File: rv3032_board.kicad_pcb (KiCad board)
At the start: 2 copper layers, 13.8 x 14.5 mm, 7 parts, among them J1 Conn_01x05_Pin, U1 RV-3032

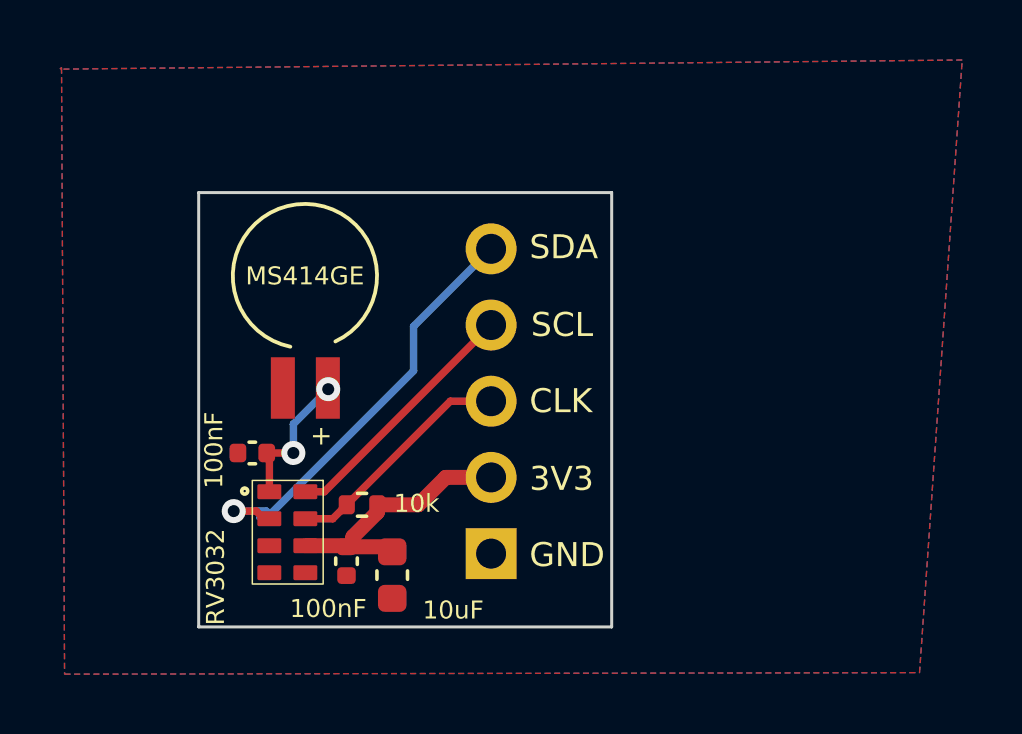
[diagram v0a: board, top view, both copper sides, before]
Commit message: v2: replacement DS3231
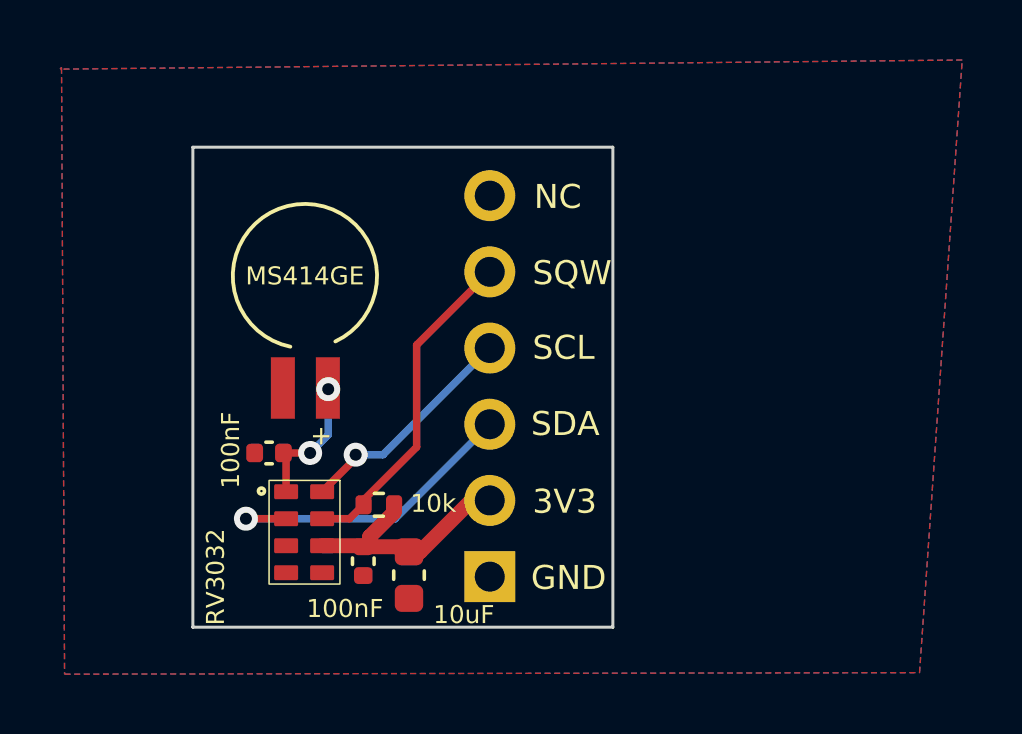
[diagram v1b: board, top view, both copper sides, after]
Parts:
- J1: value Conn_01x05_Pin -> Conn_01x06_Pin; footprint Connector_PinHeader_2.54mm:PinHeader_1x05_P2.54mm_Horizontal -> Connector_PinHeader_2.54mm:PinHeader_1x06_P2.54mm_Horizontal
- moved J1 0.77 mm to (164.9, 80.3)
- moved C3 0.56 mm to (157.5, 76.2)
- moved R1 0.56 mm to (161.2, 77.9)
- moved C1 0.56 mm to (162.2, 80.3)
- moved C2 0.56 mm to (160.7, 79.8)
- moved U1 0.56 mm to (158.7, 78.8)
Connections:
- J1 pad 3: RTC_SQW -> I2C_SDA_OTHER
- J1 pad 5: I2C_SDA_OTHER -> RTC_SQW
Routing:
- net I2C_SDA_OTHER: track 15.0 -> 10.8 mm
- net RTC_SQW: track 7.81 -> 11.1 mm
- net +3V3: track 8.92 -> 8.15 mm
- net I2C_SCL_OTHER: track 8.49 -> 7.75 mm, vias 0 -> 1
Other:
- board size 13.8 x 14.5 mm -> 14 x 16 mm
- board text added: "NC"
- board text added: "SQW"
- board text removed: "CLK"

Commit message: v1 ordered
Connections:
- J1 pad 6: unconnected-(J1-Pin_6-Pad6) -> RTC_INT
- U1 pad 3: unconnected-(U1-~{INT}-Pad3) -> RTC_INT
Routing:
- net RTC_INT: track 0.00 -> 20.4 mm, vias 0 -> 1
- net Net-(BT1-+): track 4.59 -> 4.63 mm, vias 2 -> 0
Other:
- board text added: "INT"
- board text added: "V1"
- board text removed: "NC"
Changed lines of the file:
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@@
   (net 4 "RTC_SQW")
   (net 5 "I2C_SDA_OTHER")
-  (net 6 "unconnected-(U1-~{INT}-Pad3)")
+  (net 6 "RTC_INT")
   (net 7 "unconnected-(U1-EVI-Pad4)")
   (net 8 "I2C_SCL_OTHER")
-  (net 9 "unconnected-(J1-Pin_6-Pad6)")
   (footprint "MyFootprints:BAT_MS414GE-FL26E" (layer "F.Cu")
     (at 158.75 70.3006 -90)
@@
         (effects (font (size 0.6 0.6) (thickness 0.15)))
     )
-    (fp_text user "+" (at 5.334 -0.508 90) (layer "F.SilkS")
+    (fp_text user "+" (at 3.7404 -1.7526 90) (layer "F.SilkS")
         (effects (font (size 0.64 0.64) (thickness 0.15)))
     )
@@
       (net 5 "I2C_SDA_OTHER") (pinfunction "SDA") (pintype "bidirectional") (thermal_bridge_angle 45))
     (pad "3" smd roundrect (at 0.45 0.6 90) (size 0.5 0.8) (layers "F.Cu" "F.Paste" "F.Mask") (roundrect_rratio 0.1)
-      (net 6 "unconnected-(U1-~{INT}-Pad3)") (pinfunction "~{INT}") (pintype "open_collector+no_connect") (thermal_bridge_angle 45))
+      (net 6 "RTC_INT") (pinfunction "~{INT}") (pintype "open_collector") (thermal_bridge_angle 45))
     (pad "4" smd roundrect (at 1.35 0.6 90) (size 0.5 0.8) (layers "F.Cu" "F.Paste" "F.Mask") (roundrect_rratio 0.1)
       (net 7 "unconnected-(U1-EVI-Pad4)") (pinfunction "EVI") (pintype "input+no_connect") (thermal_bridge_angle 45))
@@
         (effects (font (size 1 1) (thickness 0.15)))
     )
-    (fp_text value "10k" (at 1.8192 -0.0436) (layer "F.SilkS")
+    (fp_text value "10k" (at 1.7684 -0.5516) (layer "F.SilkS")
         (effects (font (size 0.6 0.6) (thickness 0.15)))
     )
@@
       (net 4 "RTC_SQW") (pinfunction "Pin_5") (pintype "passive"))
     (pad "6" thru_hole oval (at 0 -12.7) (size 1.7 1.7) (drill 1) (layers "*.Cu" "*.Mask")
-      (net 9 "unconnected-(J1-Pin_6-Pad6)") (pinfunction "Pin_6") (pintype "passive+no_connect"))
+      (net 6 "RTC_INT") (pinfunction "Pin_6") (pintype "passive"))
     (model "${KICAD6_3DMODEL_DIR}/Connector_PinHeader_2.54mm.3dshapes/PinHeader_1x06_P2.54mm_Horizontal.wrl"
       (offset (xyz 0 0 0))
@@
   (gr_rect (start 155 66) (end 169 82)
     (stroke (width 0.1) (type default)) (fill none) (layer "Edge.Cuts"))
-  (gr_text "RV3032" (at 162.306 69.5452) (layer "B.SilkS")
+  (gr_text "RV3032" (at 162.814 72.3646) (layer "B.SilkS")
     (effects (font (size 1 1) (thickness 0.15)) (justify left bottom mirror))
   )
-  (gr_text "NC" (at 166.37 68.1228) (layer "F.SilkS")
+  (gr_text "V1" (at 162.6616 74.0156) (layer "B.SilkS")
+    (effects (font (size 0.7 0.7) (thickness 0.1)) (justify left bottom mirror))
+  )
+  (gr_text "INT" (at 166.37 68.1228) (layer "F.SilkS")
     (effects (font (size 0.8 0.8) (thickness 0.15)) (justify left bottom))
   )
@@
     (style (thickness 0.15) (arrow_length 1.27) (text_position_mode 0) (extension_height 0.58642) (extension_offset 0.5) keep_text_aligned)
   )
+  (segment (start 159.5 75.601897) (end 159.5 74.0256) (width 0.25) (layer "F.Cu") (net 1))
   (segment (start 158.1088 76.2812) (end 158.0204 76.1928) (width 0.25) (layer "F.Cu") (net 1))
   (segment (start 158.1088 77.4844) (end 158.1088 76.2812) (width 0.25) (layer "F.Cu") (net 1))
+  (segment (start 158.909097 76.1928) (end 159.5 75.601897) (width 0.25) (layer "F.Cu") (net 1))
   (segment (start 158.0204 76.1928) (end 158.909097 76.1928) (width 0.25) (layer "F.Cu") (net 1))
-  (via (at 159.512 74.0664) (size 0.8) (drill 0.4) (layers "F.Cu" "B.Cu") (net 1))
-  (via (at 158.909097 76.1928) (size 0.8) (drill 0.4) (layers "F.Cu" "B.Cu") (net 1))
-  (segment (start 159.512 75.589897) (end 158.909097 76.1928) (width 0.25) (layer "B.Cu") (net 1))
-  (segment (start 159.512 74.0664) (end 159.512 75.589897) (width 0.25) (layer "B.Cu") (net 1))
   (segment (start 160.8932 78.9868) (end 161.708 78.172) (width 0.5) (layer "F.Cu") (net 3))
   (segment (start 160.858 79.2844) (end 160.8932 79.3196) (width 0.5) (layer "F.Cu") (net 3))
@@
   (segment (start 159.3088 78.3844) (end 160.2236 78.3844) (width 0.25) (layer "F.Cu") (net 4))
   (segment (start 162.4584 72.5932) (end 164.8968 70.1548) (width 0.25) (layer "F.Cu") (net 4))
-  (segment (start 158.1088 78.3844) (end 156.7688 78.3844) (width 0.25) (layer "F.Cu") (net 5))
-  (via (at 156.7688 78.3844) (size 0.8) (drill 0.4) (layers "F.Cu" "B.Cu") (net 5))
-  (segment (start 156.7688 78.3844) (end 161.7472 78.3844) (width 0.25) (layer "B.Cu") (net 5))
+  (segment (start 156.7434 78.1304) (end 156.9974 78.3844) (width 0.25) (layer "F.Cu") (net 5))
+  (segment (start 156.9974 78.3844) (end 158.1088 78.3844) (width 0.25) (layer "F.Cu") (net 5))
+  (via (at 156.7434 78.1304) (size 0.8) (drill 0.4) (layers "F.Cu" "B.Cu") (net 5))
+  (segment (start 156.9974 78.3844) (end 161.7472 78.3844) (width 0.25) (layer "B.Cu") (net 5))
   (segment (start 161.7472 78.3844) (end 164.8968 75.2348) (width 0.25) (layer "B.Cu") (net 5))
+  (segment (start 156.7434 78.1304) (end 156.9974 78.3844) (width 0.25) (layer "B.Cu") (net 5))
+  (segment (start 156.7688 79.4766) (end 156.7942 79.4512) (width 0.25) (layer "F.Cu") (net 6))
+  (segment (start 156.7688 79.4512) (end 156.7688 79.4766) (width 0.25) (layer "F.Cu") (net 6))
+  (segment (start 156.7942 79.4512) (end 156.7688 79.4512) (width 0.25) (layer "F.Cu") (net 6))
+  (segment (start 158.1088 79.2844) (end 156.961 79.2844) (width 0.25) (layer "F.Cu") (net 6))
+  (segment (start 156.961 79.2844) (end 156.7942 79.4512) (width 0.25) (layer "F.Cu") (net 6))
+  (via (at 156.7688 79.4512) (size 0.8) (drill 0.4) (layers "F.Cu" "B.Cu") (net 6))
+  (segment (start 156.7688 79.4512) (end 155.9052 78.5876) (width 0.25) (layer "B.Cu") (net 6))
+  (segment (start 158.496 68.9102) (end 163.6014 68.9102) (width 0.25) (layer "B.Cu") (net 6))
+  (segment (start 163.6014 68.9102) (end 164.8968 67.6148) (width 0.25) (layer "B.Cu") (net 6))
+  (segment (start 155.9052 71.501) (end 158.496 68.9102) (width 0.25) (layer "B.Cu") (net 6))
+  (segment (start 155.9052 78.5876) (end 155.9052 71.501) (width 0.25) (layer "B.Cu") (net 6))
   (segment (start 160.4772 76.316) (end 160.4264 76.2508) (width 0.25) (layer "F.Cu") (net 8))
   (segment (start 159.3088 77.4844) (end 160.4772 76.316) (width 0.25) (layer "F.Cu") (net 8))
